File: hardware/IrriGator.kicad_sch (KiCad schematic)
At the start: 45 parts, among them J1 230VAC, J2 24VAC L, J3 24VAC N, J4 24VAC, J5 Conn_01x04_Socket, J6 Conn_01x04_Pin, J7 Conn_01x04_Pin, SW1 SW_Push, T1 24V 16VA, U1 LF33_TO220, U2 ESP-01v090, U3 DS3231-MINI-RTC, U4 ATtiny45-20P, U5 ATtiny45-20P

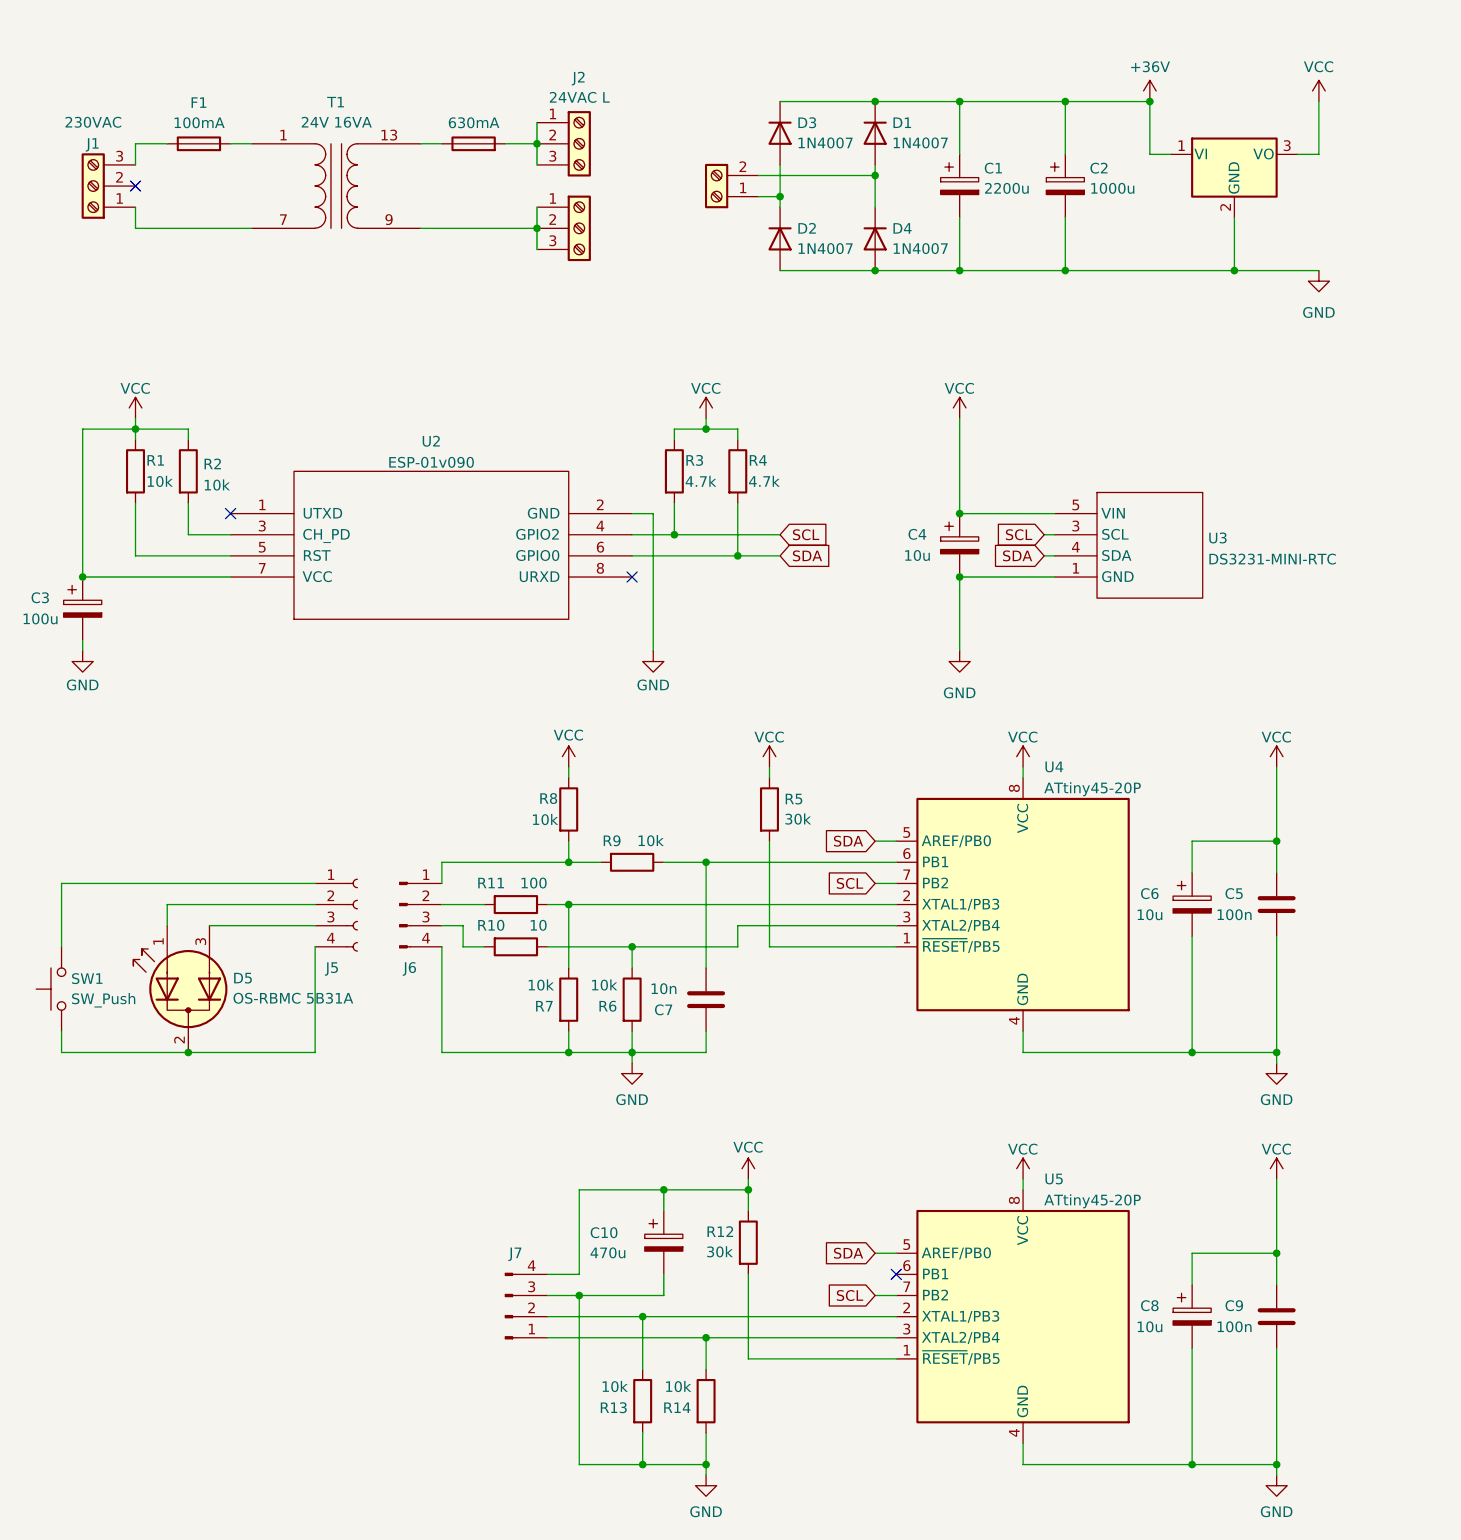
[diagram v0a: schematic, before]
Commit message: Moved rectifier part to the transformer module, DC-DC stepdown becomes an external module
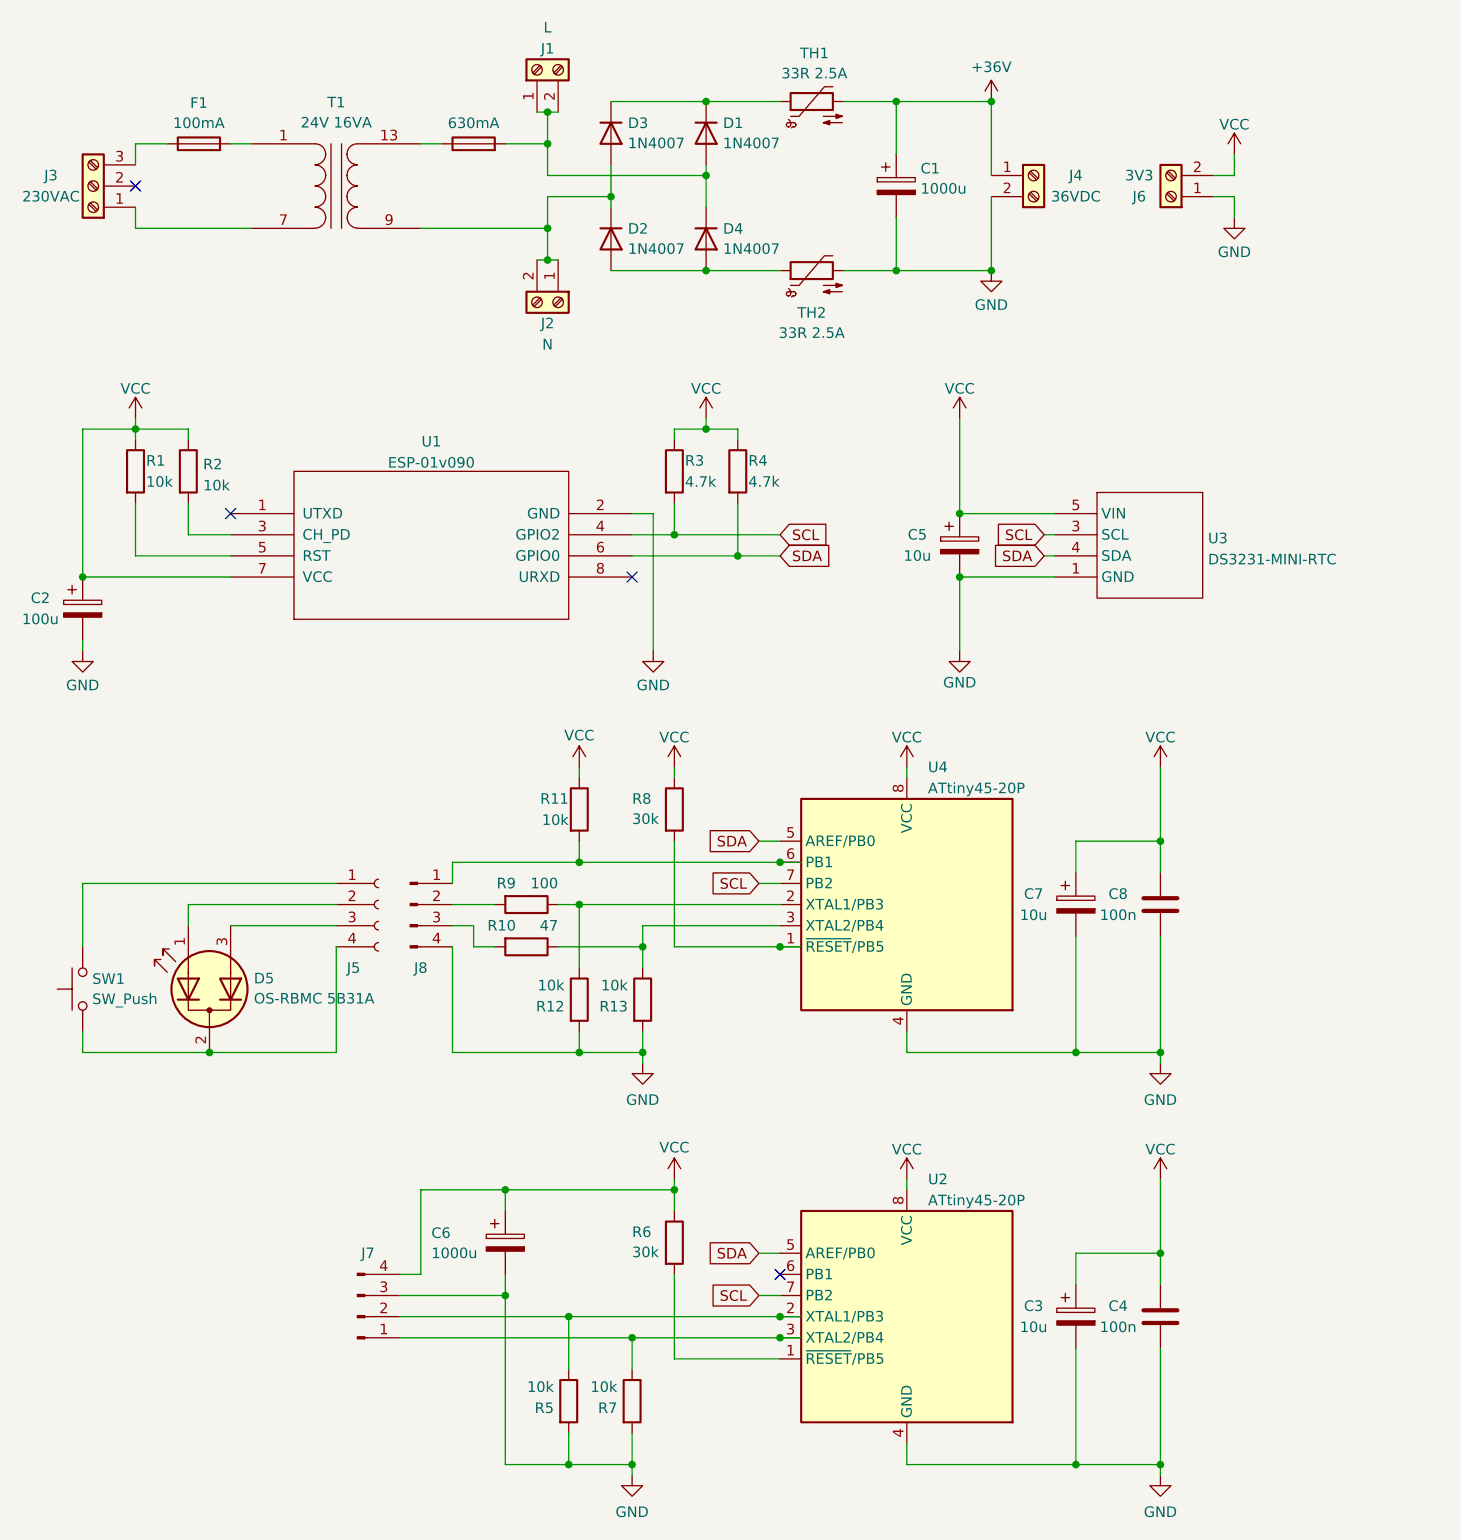
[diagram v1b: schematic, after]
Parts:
- removed C2: 1000u, Capacitor_THT:CP_Radial_D16.0mm_P7.50mm, symbol Device:C_Polarized
- removed C7: 10n, Capacitor_THT:C_Disc_D3.0mm_W1.6mm_P2.50mm, symbol Device:C
- removed J2: 24VAC L, TerminalBlock_Phoenix:TerminalBlock_Phoenix_MKDS-1,5-3-5.08_1x03_P5.08mm_Horizontal, symbol Connector:Screw_Terminal_01x03
- removed J3: 24VAC N, TerminalBlock_Phoenix:TerminalBlock_Phoenix_MKDS-1,5-3-5.08_1x03_P5.08mm_Horizontal, symbol Connector:Screw_Terminal_01x03
- removed R9: 10k, Resistor_THT:R_Axial_DIN0204_L3.6mm_D1.6mm_P7.62mm_Horizontal, symbol Device:R
- removed U1: LF33_TO220, Package_TO_SOT_THT:TO-220-3_Vertical, symbol Regulator_Linear:LF33_TO220
- added J1: L, TerminalBlock_Phoenix:TerminalBlock_Phoenix_MKDS-1,5-2-5.08_1x02_P5.08mm_Horizontal, symbol Connector:Screw_Terminal_01x02
- added J2: N, TerminalBlock_Phoenix:TerminalBlock_Phoenix_MKDS-1,5-2-5.08_1x02_P5.08mm_Horizontal, symbol Connector:Screw_Terminal_01x02
- added J6: 3V3, TerminalBlock_Phoenix:TerminalBlock_Phoenix_MKDS-1,5-2-5.08_1x02_P5.08mm_Horizontal, symbol Connector:Screw_Terminal_01x02
- added TH1, TH2: 33R 2.5A, Varistor:RV_Disc_D15.5mm_W6.8mm_P7.5mm, symbol Device:Thermistor_NTC
- C1: value 2200u -> 1000u
- C6: renamed from C10; value 470u -> 1000u
- J4: value 24VAC -> 36VDC
- R10: value 10 -> 47
- renumbered C3 to C2, C8 to C3, C9 to C4, C4 to C5, C6 to C7, C5 to C8, J1 to J3, J6 to J8, R8 to R11, R7 to R12, R6 to R13, R13 to R5, R12 to R6, R14 to R7, R5 to R8, R11 to R9, U2 to U1, U5 to U2
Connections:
- net +36V: now also J4.1 (Pin_1), TH1.2; no longer D1.1 (K), D3.1 (K)
- net GND: now also J4.2 (Pin_2), J6.1 (Pin_1), TH2.2; no longer D2.2 (A), D4.2 (A)
- net VCC: now also J6.2 (Pin_2)
- net at T1.9 (SA): now also D2.1 (K), D3.2 (A), J2.1 (Pin_1), J2.2 (Pin_2)
- net at J8.1 (Pin_1), R11.2: now also U4.6 (PB1)
- net at D1.2 (A), D4.1 (K): now also F2.2, J1.1 (Pin_1), J1.2 (Pin_2); no longer J4.2 (Pin_2)
- new net: D2.2 (A), D4.2 (A), TH2.1
- new net: D1.1 (K), D3.1 (K), TH1.1
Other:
- moved on the sheet: C1, C3, C4, C6, C7, C8, D1, D2, D3, D4, D5, J5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
